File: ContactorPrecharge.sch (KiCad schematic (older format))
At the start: 9 parts

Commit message: basic connectivity
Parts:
- added R? (x5): R, symbol R
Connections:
- wire segments 0 -> 28
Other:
- moved on the sheet: D?, Q?, U?
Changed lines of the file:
@@
 LIBS:contrib
 LIBS:valves
+LIBS:ContactorPrecharge-cache
 EELAYER 25 0
 EELAYER END
@@
 F 3 "" H 6250 5000 50  0000 C CNN
 	1    6250 5000
-	1    0    0    -1
+	-1   0    0    -1
 $EndComp
 $Comp
 L OPTO-TRANSISTOR U?
 U 1 1 56F0DEFB
-P 7900 5300
-F 0 "U?" H 7700 5500 50  0000 L CNN
-F 1 "OPTO-TRANSISTOR" H 7700 5100 50  0000 L CNN
-F 2 "" H 7700 5100 50  0000 L CIN
-F 3 "" H 7900 5300 50  0000 L CNN
-	1    7900 5300
+P 7850 5050
+F 0 "U?" H 7650 5250 50  0000 L CNN
+F 1 "OPTO-TRANSISTOR" H 7650 4850 50  0000 L CNN
+F 2 "" H 7650 4850 50  0000 L CIN
+F 3 "" H 7850 5050 50  0000 L CNN
+	1    7850 5050
 	-1   0    0    -1
 $EndComp
@@
 L MOC3021M U?
 U 1 1 56F0DF72
-P 8050 3200
-F 0 "U?" H 7840 3390 50  0000 L CNN
-F 1 "MOC3021M" H 8050 3400 50  0000 L CNN
-F 2 "DIP-6" H 7850 3000 50  0000 L CIN
-F 3 "" H 8025 3200 50  0000 L CNN
-	1    8050 3200
+P 8100 4050
+F 0 "U?" H 7890 4240 50  0000 L CNN
+F 1 "MOC3021M" H 8100 4250 50  0000 L CNN
+F 2 "DIP-6" H 7900 3850 50  0000 L CIN
+F 3 "" H 8075 4050 50  0000 L CNN
+	1    8100 4050
 	1    0    0    -1
 $EndComp
@@
 L Q_PNP_BCE Q?
 U 1 1 56F0E04D
-P 5150 3850
-F 0 "Q?" H 5450 3900 50  0000 R CNN
-F 1 "Q_PNP_BCE" H 5750 3800 50  0000 R CNN
-F 2 "" H 5350 3950 50  0000 C CNN
-F 3 "" H 5150 3850 50  0000 C CNN
-	1    5150 3850
+P 4950 4100
+F 0 "Q?" H 5250 4150 50  0000 R CNN
+F 1 "Q_PNP_BCE" H 5550 4050 50  0000 R CNN
+F 2 "" H 5150 4200 50  0000 C CNN
+F 3 "" H 4950 4100 50  0000 C CNN
+	1    4950 4100
 	-1   0    0    1
 $EndComp
@@
 L Q_NPN_BCE Q?
 U 1 1 56F0E0BE
-P 8650 3050
-F 0 "Q?" H 8950 3100 50  0000 R CNN
-F 1 "Q_NPN_BCE" H 9250 3000 50  0000 R CNN
-F 2 "" H 8850 3150 50  0000 C CNN
-F 3 "" H 8650 3050 50  0000 C CNN
-	1    8650 3050
+P 8750 4150
+F 0 "Q?" H 9050 4200 50  0000 R CNN
+F 1 "Q_NPN_BCE" H 9350 4100 50  0000 R CNN
+F 2 "" H 8950 4250 50  0000 C CNN
+F 3 "" H 8750 4150 50  0000 C CNN
+	1    8750 4150
 	1    0    0    -1
 $EndComp
@@
 L D D?
 U 1 1 56F0E506
-P 10000 3800
-F 0 "D?" H 10000 3900 50  0000 C CNN
-F 1 "D" H 10000 3700 50  0000 C CNN
-F 2 "" H 10000 3800 50  0000 C CNN
-F 3 "" H 10000 3800 50  0000 C CNN
-	1    10000 3800
+P 10000 4250
+F 0 "D?" H 10000 4350 50  0000 C CNN
+F 1 "D" H 10000 4150 50  0000 C CNN
+F 2 "" H 10000 4250 50  0000 C CNN
+F 3 "" H 10000 4250 50  0000 C CNN
+	1    10000 4250
 	1    0    0    -1
 $EndComp
@@
 L D D?
 U 1 1 56F0E5AD
-P 9850 3950
-F 0 "D?" H 9850 4050 50  0000 C CNN
-F 1 "D" H 9850 3850 50  0000 C CNN
-F 2 "" H 9850 3950 50  0000 C CNN
-F 3 "" H 9850 3950 50  0000 C CNN
-	1    9850 3950
+P 9850 4400
+F 0 "D?" H 9850 4500 50  0000 C CNN
+F 1 "D" H 9850 4300 50  0000 C CNN
+F 2 "" H 9850 4400 50  0000 C CNN
+F 3 "" H 9850 4400 50  0000 C CNN
+	1    9850 4400
 	0    1    1    0
 $EndComp
@@
 L D D?
 U 1 1 56F0E5FE
-P 10000 4100
-F 0 "D?" H 10000 4200 50  0000 C CNN
-F 1 "D" H 10000 4000 50  0000 C CNN
-F 2 "" H 10000 4100 50  0000 C CNN
-F 3 "" H 10000 4100 50  0000 C CNN
-	1    10000 4100
+P 10000 4550
+F 0 "D?" H 10000 4650 50  0000 C CNN
+F 1 "D" H 10000 4450 50  0000 C CNN
+F 2 "" H 10000 4550 50  0000 C CNN
+F 3 "" H 10000 4550 50  0000 C CNN
+	1    10000 4550
 	1    0    0    -1
 $EndComp
@@
 L D D?
 U 1 1 56F0E64E
-P 10150 3950
-F 0 "D?" H 10150 4050 50  0000 C CNN
-F 1 "D" H 10150 3850 50  0000 C CNN
-F 2 "" H 10150 3950 50  0000 C CNN
-F 3 "" H 10150 3950 50  0000 C CNN
-	1    10150 3950
+P 10150 4400
+F 0 "D?" H 10150 4500 50  0000 C CNN
+F 1 "D" H 10150 4300 50  0000 C CNN
+F 2 "" H 10150 4400 50  0000 C CNN
+F 3 "" H 10150 4400 50  0000 C CNN
+	1    10150 4400
 	0    1    1    0
 $EndComp
+$Comp
+L R R?
+U 1 1 56F0F035
+P 5450 4850
+F 0 "R?" V 5530 4850 50  0000 C CNN
+F 1 "R" V 5450 4850 50  0000 C CNN
+F 2 "" V 5380 4850 50  0000 C CNN
+F 3 "" H 5450 4850 50  0000 C CNN
+	1    5450 4850
+	1    0    0    -1
+$EndComp
+Wire Wire Line
+	5450 5000 5750 5000
+Wire Wire Line
+	5150 4100 5450 4100
+Wire Wire Line
+	5450 4100 5450 4700
+Wire Wire Line
+	5750 5200 5600 5200
+Wire Wire Line
+	5600 5200 5600 4500
+Wire Wire Line
+	5600 4500 6900 4500
+Wire Wire Line
+	6900 4500 6900 4800
+Wire Wire Line
+	6750 4800 7300 4800
+Wire Wire Line
+	7300 5050 7550 5050
+Wire Wire Line
+	7300 4600 7300 5050
+Connection ~ 6900 4800
+$Comp
+L R R?
+U 1 1 56F0F2E6
+P 7300 4450
+F 0 "R?" V 7380 4450 50  0000 C CNN
+F 1 "R" V 7300 4450 50  0000 C CNN
+F 2 "" V 7230 4450 50  0000 C CNN
+F 3 "" H 7300 4450 50  0000 C CNN
+	1    7300 4450
+	1    0    0    -1
+$EndComp
+Connection ~ 7300 4800
+Wire Wire Line
+	7300 4300 7300 3900
+Wire Wire Line
+	7300 3900 4850 3900
+$Comp
+L R R?
+U 1 1 56F0F46B
+P 8850 4650
+F 0 "R?" V 8930 4650 50  0000 C CNN
+F 1 "R" V 8850 4650 50  0000 C CNN
+F 2 "" V 8780 4650 50  0000 C CNN
+F 3 "" H 8850 4650 50  0000 C CNN
+	1    8850 4650
+	1    0    0    -1
+$EndComp
+$Comp
+L R R?
+U 1 1 56F0F4DF
+P 8850 5150
+F 0 "R?" V 8930 5150 50  0000 C CNN
+F 1 "R" V 8850 5150 50  0000 C CNN
+F 2 "" V 8780 5150 50  0000 C CNN
+F 3 "" H 8850 5150 50  0000 C CNN
+	1    8850 5150
+	1    0    0    -1
+$EndComp
+Wire Wire Line
+	8400 3950 9850 3950
+Wire Wire Line
+	8550 4150 8400 4150
+Wire Wire Line
+	8850 4500 8850 4350
+Wire Wire Line
+	8850 5000 8850 4800
+$Comp
+L R R?
+U 1 1 56F0F6F1
+P 8550 4950
+F 0 "R?" V 8630 4950 50  0000 C CNN
+F 1 "R" V 8550 4950 50  0000 C CNN
+F 2 "" V 8480 4950 50  0000 C CNN
+F 3 "" H 8550 4950 50  0000 C CNN
+	1    8550 4950
+	0    1    1    0
+$EndComp
+Wire Wire Line
+	8700 4950 8850 4950
+Connection ~ 8850 4950
+Wire Wire Line
+	9850 3950 9850 4250
+Connection ~ 8850 3950
+Wire Wire Line
+	10150 5300 10150 4550
+Wire Wire Line
+	8150 5300 10150 5300
+Wire Wire Line
+	8150 5150 8150 5300
+Connection ~ 8850 5300
+Wire Wire Line
+	8400 4950 8150 4950
+Wire Wire Line
+	7550 5150 7300 5150
+Wire Wire Line
+	7300 5150 7300 5500
+Wire Wire Line
+	7300 5500 4850 5500
+Wire Wire Line
+	4850 5500 4850 4750
+Wire Wire Line
+	4850 4300 4850 4500
+Wire Wire Line
+	7800 3950 7300 3950
+Connection ~ 7300 3950
 $EndSCHEMATC

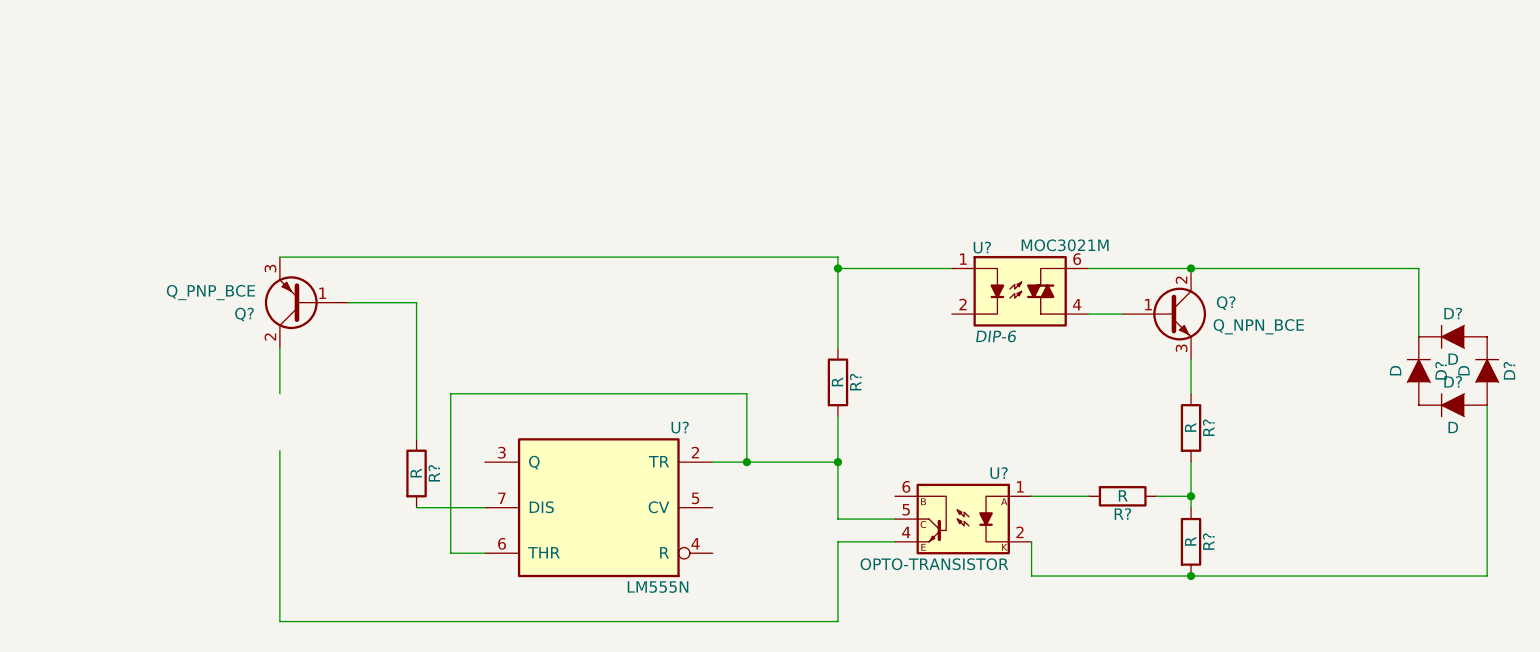
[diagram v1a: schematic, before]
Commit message: added LEDs
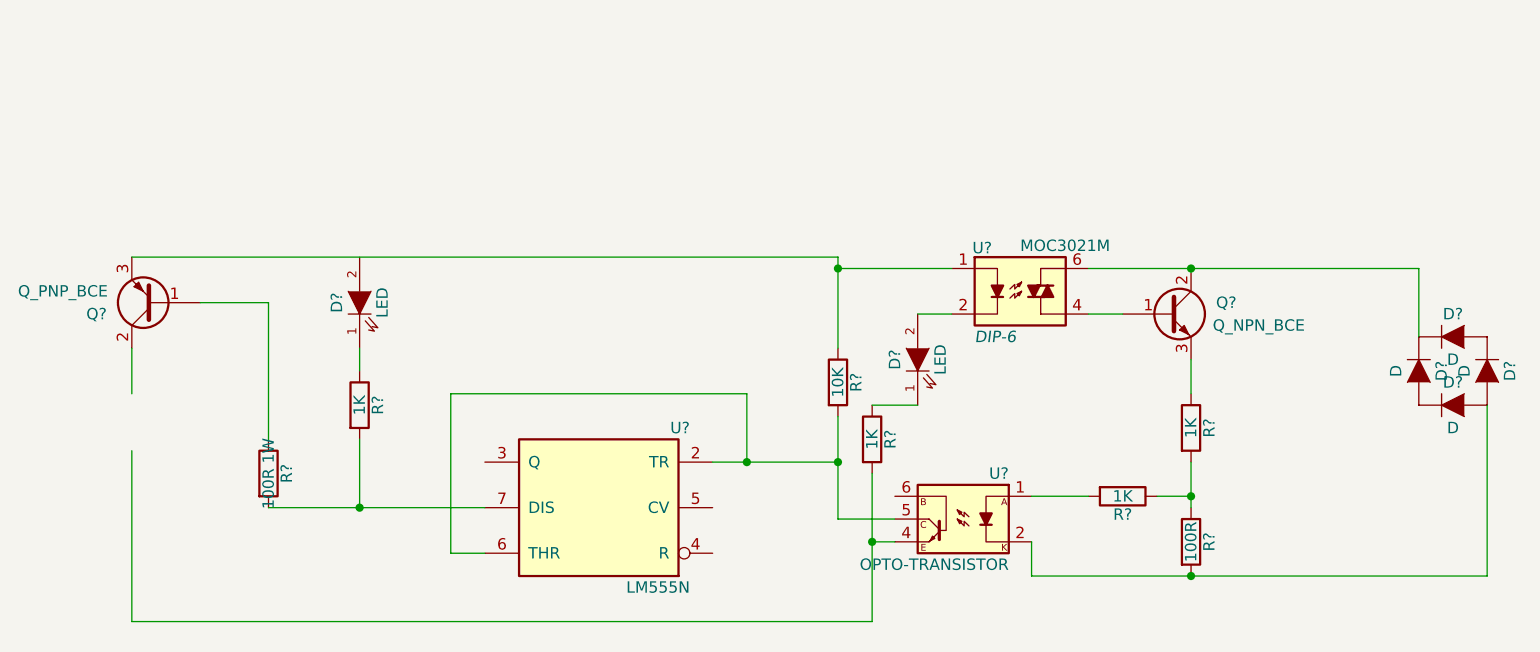
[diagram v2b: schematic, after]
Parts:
- added D? (x2): LED, symbol LED
- added R? (x2): 1K, symbol R
- R?: value R -> 100R 1W
- R?: value R -> 10K
- R? (x2): value R -> 1K
- R?: value R -> 100R
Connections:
- wire segments 28 -> 32
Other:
- moved on the sheet: Q?, R?
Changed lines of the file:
@@
 L Q_PNP_BCE Q?
 U 1 1 56F0E04D
-P 4950 4100
-F 0 "Q?" H 5250 4150 50  0000 R CNN
-F 1 "Q_PNP_BCE" H 5550 4050 50  0000 R CNN
-F 2 "" H 5150 4200 50  0000 C CNN
-F 3 "" H 4950 4100 50  0000 C CNN
-	1    4950 4100
+P 4300 4100
+F 0 "Q?" H 4600 4150 50  0000 R CNN
+F 1 "Q_PNP_BCE" H 4900 4050 50  0000 R CNN
+F 2 "" H 4500 4200 50  0000 C CNN
+F 3 "" H 4300 4100 50  0000 C CNN
+	1    4300 4100
 	-1   0    0    1
 $EndComp
@@
 L R R?
 U 1 1 56F0F035
-P 5450 4850
-F 0 "R?" V 5530 4850 50  0000 C CNN
-F 1 "R" V 5450 4850 50  0000 C CNN
-F 2 "" V 5380 4850 50  0000 C CNN
-F 3 "" H 5450 4850 50  0000 C CNN
-	1    5450 4850
-	1    0    0    -1
-$EndComp
-Wire Wire Line
-	5450 5000 5750 5000
-Wire Wire Line
-	5150 4100 5450 4100
-Wire Wire Line
-	5450 4100 5450 4700
+P 4800 4850
+F 0 "R?" V 4880 4850 50  0000 C CNN
+F 1 "100R 1W" V 4800 4850 50  0000 C CNN
+F 2 "" V 4730 4850 50  0000 C CNN
+F 3 "" H 4800 4850 50  0000 C CNN
+	1    4800 4850
+	1    0    0    -1
+$EndComp
+Wire Wire Line
+	4800 5000 5750 5000
+Wire Wire Line
+	4500 4100 4800 4100
+Wire Wire Line
+	4800 4100 4800 4700
 Wire Wire Line
 	5750 5200 5600 5200
@@
 P 7300 4450
 F 0 "R?" V 7380 4450 50  0000 C CNN
-F 1 "R" V 7300 4450 50  0000 C CNN
+F 1 "10K" V 7300 4450 50  0000 C CNN
 F 2 "" V 7230 4450 50  0000 C CNN
 F 3 "" H 7300 4450 50  0000 C CNN
@@
 Connection ~ 7300 4800
 Wire Wire Line
-	7300 4300 7300 3900
-Wire Wire Line
-	7300 3900 4850 3900
+	7300 3900 7300 4300
+Wire Wire Line
+	7300 3900 4200 3900
 $Comp
 L R R?
@@
 P 8850 4650
 F 0 "R?" V 8930 4650 50  0000 C CNN
-F 1 "R" V 8850 4650 50  0000 C CNN
+F 1 "1K" V 8850 4650 50  0000 C CNN
 F 2 "" V 8780 4650 50  0000 C CNN
 F 3 "" H 8850 4650 50  0000 C CNN
@@
 P 8850 5150
 F 0 "R?" V 8930 5150 50  0000 C CNN
-F 1 "R" V 8850 5150 50  0000 C CNN
+F 1 "100R" V 8850 5150 50  0000 C CNN
 F 2 "" V 8780 5150 50  0000 C CNN
 F 3 "" H 8850 5150 50  0000 C CNN
@@
 	8850 4500 8850 4350
 Wire Wire Line
-	8850 5000 8850 4800
+	8850 4800 8850 5000
 $Comp
 L R R?
@@
 P 8550 4950
 F 0 "R?" V 8630 4950 50  0000 C CNN
-F 1 "R" V 8550 4950 50  0000 C CNN
+F 1 "1K" V 8550 4950 50  0000 C CNN
 F 2 "" V 8480 4950 50  0000 C CNN
 F 3 "" H 8550 4950 50  0000 C CNN
@@
 	8400 4950 8150 4950
 Wire Wire Line
-	7550 5150 7300 5150
-Wire Wire Line
-	7300 5150 7300 5500
-Wire Wire Line
-	7300 5500 4850 5500
-Wire Wire Line
-	4850 5500 4850 4750
-Wire Wire Line
-	4850 4300 4850 4500
+	4200 5500 7450 5500
+Wire Wire Line
+	4200 5500 4200 4750
+Wire Wire Line
+	4200 4300 4200 4500
 Wire Wire Line
 	7800 3950 7300 3950
 Connection ~ 7300 3950
+$Comp
+L LED D?
+U 1 1 56F0E96A
+P 5200 4100
+F 0 "D?" H 5200 4200 50  0000 C CNN
+F 1 "LED" H 5200 4000 50  0000 C CNN
+F 2 "" H 5200 4100 50  0000 C CNN
+F 3 "" H 5200 4100 50  0000 C CNN
+	1    5200 4100
+	0    -1   -1   0
+$EndComp
+$Comp
+L R R?
+U 1 1 56F0E9FE
+P 5200 4550
+F 0 "R?" V 5280 4550 50  0000 C CNN
+F 1 "1K" V 5200 4550 50  0000 C CNN
+F 2 "" V 5130 4550 50  0000 C CNN
+F 3 "" H 5200 4550 50  0000 C CNN
+	1    5200 4550
+	1    0    0    -1
+$EndComp
+Wire Wire Line
+	5200 4400 5200 4300
+Wire Wire Line
+	5200 4700 5200 5000
+Connection ~ 5200 5000
+$Comp
+L LED D?
+U 1 1 56F0EB78
+P 7650 4350
+F 0 "D?" H 7650 4450 50  0000 C CNN
+F 1 "LED" H 7650 4250 50  0000 C CNN
+F 2 "" H 7650 4350 50  0000 C CNN
+F 3 "" H 7650 4350 50  0000 C CNN
+	1    7650 4350
+	0    -1   -1   0
+$EndComp
+Wire Wire Line
+	7800 4150 7650 4150
+Wire Wire Line
+	7650 4550 7450 4550
+$Comp
+L R R?
+U 1 1 56F0EED5
+P 7450 4700
+F 0 "R?" V 7530 4700 50  0000 C CNN
+F 1 "1K" V 7450 4700 50  0000 C CNN
+F 2 "" V 7380 4700 50  0000 C CNN
+F 3 "" H 7450 4700 50  0000 C CNN
+	1    7450 4700
+	1    0    0    -1
+$EndComp
+Wire Wire Line
+	7450 5500 7450 4850
+Wire Wire Line
+	7550 5150 7450 5150
+Connection ~ 7450 5150
 $EndSCHEMATC
